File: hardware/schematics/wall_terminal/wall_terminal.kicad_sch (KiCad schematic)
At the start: 22 parts, among them J1 6P6C, J2 6P6C, J3 Conn_02x12_Odd_Even, J4 Reset, Q1 2N7000, U1 ATtiny13A-P, U2 MAX487E

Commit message: !refactor
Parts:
- removed JP1: INT/ADC, Jumper:SolderJumper-3_P1.3mm_Open_Pad1.0x1.5mm, symbol Jumper:SolderJumper_3_Open
- removed JP2: PWM/SIMPLE, Jumper:SolderJumper-3_P1.3mm_Open_Pad1.0x1.5mm, symbol Jumper:SolderJumper_3_Open
- removed Q1: 2N7000, Package_TO_SOT_THT:TO-92_Inline, symbol Transistor_FET:2N7000
- removed R1, R10, R2, R3, R4, R5, R6, R7, R8, R9: R, Resistor_THT:R_Axial_DIN0207_L6.3mm_D2.5mm_P2.54mm_Vertical, symbol Device:R
- removed R11: R, Resistor_THT:R_Axial_DIN0207_L6.3mm_D2.5mm_P7.62mm_Horizontal, symbol Device:R
- removed U1: ATtiny13A-P, Package_DIP:DIP-8_W7.62mm_Socket, symbol MCU_Microchip_ATtiny:ATtiny13A-P
- removed U2: MAX487E, Package_DIP:DIP-8_W7.62mm_Socket, symbol Interface_UART:MAX487E
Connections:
- net LED- is gone; now on net GND: J3.2 (Pin_2)
- net +5V: no longer J3.3 (Pin_3)
- net MCU/~{RST}: now reaches J4.2 (Pin_2)
- net LED+ renamed MCU/PWM_B
- net SW_1 renamed IN/S1
- net SW_2 renamed IN/S2
- net SW_3 renamed IN/S3
- net SW_4 renamed IN/S4
- net SW_5 renamed IN/S5
- net SW_6 renamed IN/S6
- net SW_7 renamed IN/S7
- net SW_8 renamed IN/S8
- new net MCU/PWM_A: J3.3 (Pin_3)
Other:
- added sheet IN (in.kicad_sch)
- added sheet MCU (mcu.kicad_sch)
- added sheet PERIPHERALS (peripherals.kicad_sch)
- moved on the sheet: C1, C2, J1, J2, J3

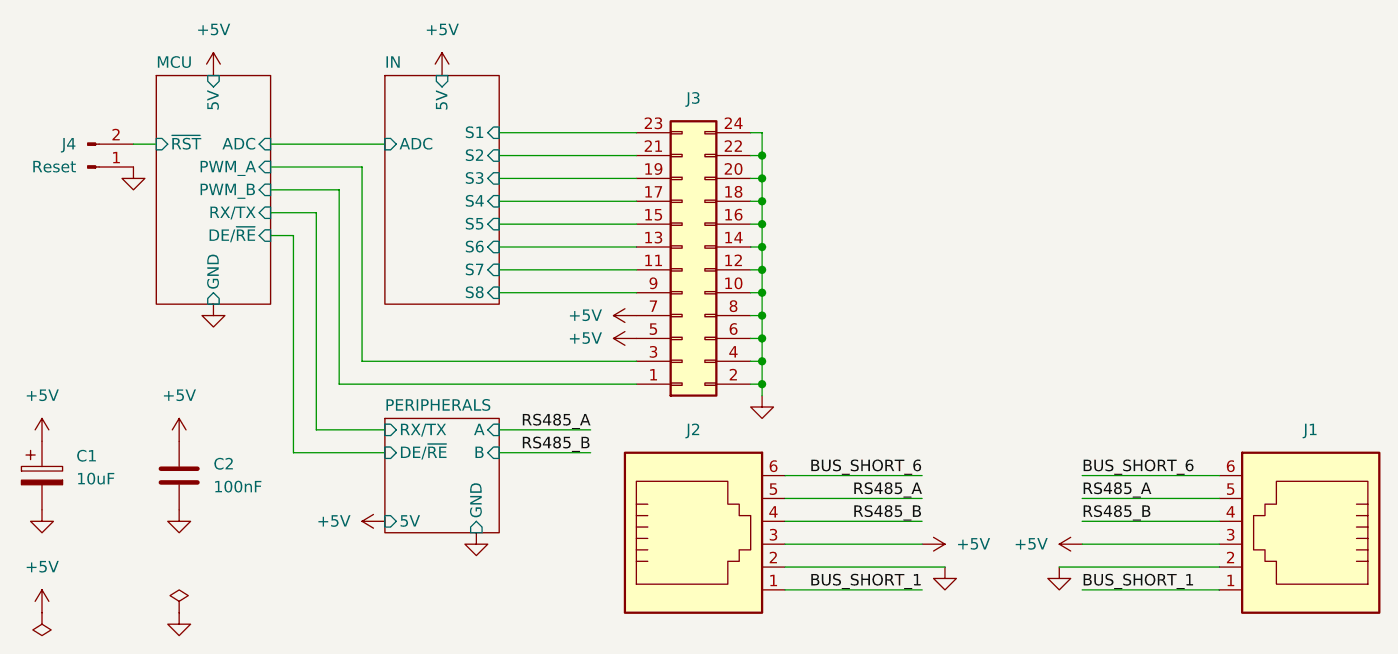
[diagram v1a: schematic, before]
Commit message: fix: added optional resistors on PWM outputs.
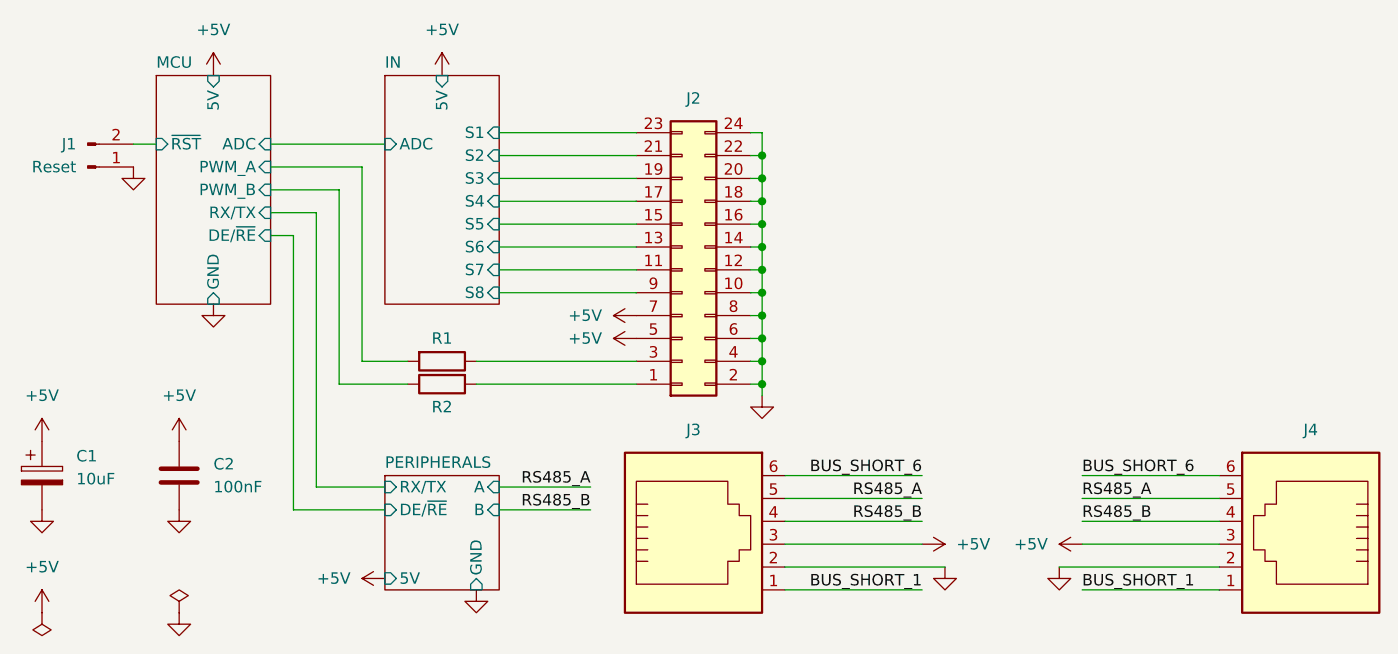
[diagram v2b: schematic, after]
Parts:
- added R1, R2: R, Resistor_THT:R_Axial_DIN0207_L6.3mm_D2.5mm_P2.54mm_Vertical, symbol Device:R
- renumbered J4 to J1, J3 to J2, J2 to J3, J1 to J4
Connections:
- net MCU/PWM_A: now also R1.2; no longer J2.3 (Pin_3)
- net MCU/PWM_B: now also R2.1; no longer J2.1 (Pin_1)
- new net: J2.3 (Pin_3), R1.1
- new net: J2.1 (Pin_1), R2.2

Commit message: docs
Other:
- note added: "!!! RIFARE LASCIANDO UN SOLO PIN ADC E PREDISPONENDO DOPPIO DIODO PER TERZO PULSANTE Sequenza fili: V, BA, A, BB, B, BV"
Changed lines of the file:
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@@
 		(title "Domoticata wall terminal")
 		(date "2024-07-12")
-		(rev "0.1")
+		(rev "0.0.1")
 		(company "Davide Scalisi")
 	)
@@
 		)
 	)
+	(text "!!! RIFARE LASCIANDO UN SOLO PIN ADC E PREDISPONENDO DOPPIO DIODO PER TERZO PULSANTE\n\nSequenza fili: V, BA, A, BB, B, BV"
+		(exclude_from_sim no)
+		(at 162.306 38.1 0)
+		(effects
+			(font
+				(size 1.27 1.27)
+			)
+		)
+	)
